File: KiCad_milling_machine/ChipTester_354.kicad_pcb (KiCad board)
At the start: 2 copper layers, 172 x 61.5 mm, 55 parts, among them U1 TLE2426xP, U2 L7805, U3 TLE2426xP, U4 TLE2426xP, U5 MCP6002-xP

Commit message: Removed Switch
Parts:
- removed C4: 1 µF, Capacitor_THT:CP_Radial_D5.0mm_P2.00mm
- removed S2: 100SP3T2B4M6RE, 100SP3T2B4M6RE:100SP3T2B4M6RE
- removed TP6: 4.5/2.25V VGND, TestPoint:TestPoint_Pad_D2.0mm
- removed U3: TLE2426xP, Package_DIP:DIP-8_W7.62mm
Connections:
- D11 pad 1: /2.5 VGND -> Net-(D10-A)
- D11 pad 2: Net-(D10-A) -> /2.5 VGND
- D13 pad 1: /2.5 VGND -> Net-(D12-A)
- D13 pad 2: Net-(D12-A) -> /2.5 VGND
- D3 pad 1: /CHIP_GND -> Net-(D2-A)
- D3 pad 2: Net-(D2-A) -> /CHIP_GND
- D5 pad 1: /CHIP_GND -> Net-(D4-A)
- D5 pad 2: Net-(D4-A) -> /CHIP_GND
- D9 pad 1: /2.5 VGND -> Net-(D8-A)
- D9 pad 2: Net-(D8-A) -> /2.5 VGND
- TP3 pad 1: /PWR Supply/VDIV -> /CHIP_GND
- U1 pad 1: /PWR Supply/VDIV -> /CHIP_GND
- U_T1 pad 7: /CHIP+ -> +9V
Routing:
- net /PWR Supply/VDIV: track 49.2 -> 0.00 mm
- net /CHIP_GND: track 56.7 -> 85.3 mm, vias 0 -> 1
- net /CHIP+: track 26.8 -> 0.00 mm
- net +9V: track 171.7 -> 185.6 mm
- net Net-(U3-NOISE_REDUCTION): track 3.76 -> 0.00 mm

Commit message: Ground inverting input of AD/INA circuit
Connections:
- U_T1 pad 2: unconnected-(U_T1---Pad2) -> GND
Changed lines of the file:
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@@
 	(net 34 "unconnected-(U5B-+-Pad5)")
 	(net 35 "unconnected-(U5B---Pad6)")
-	(net 36 "unconnected-(U_T1---Pad2)")
-	(net 37 "unconnected-(U_T1-Rg-Pad1)")
-	(net 38 "unconnected-(U_T1-Rg-Pad8)")
-	(net 39 "unconnected-(S1-Pad4)")
-	(net 40 "unconnected-(S1-Pad1)")
-	(net 41 "unconnected-(S1-PadS2)")
-	(net 42 "unconnected-(S1-PadS1)")
-	(net 43 "/AD623 and INA126/AD_O")
-	(net 44 "/MCP6002 and IF353/MCPA_O")
-	(net 45 "/MCP6002 and IF353/MCPB_O")
+	(net 36 "unconnected-(U_T1-Rg-Pad1)")
+	(net 37 "unconnected-(U_T1-Rg-Pad8)")
+	(net 38 "unconnected-(S1-Pad4)")
+	(net 39 "unconnected-(S1-Pad1)")
+	(net 40 "unconnected-(S1-PadS2)")
+	(net 41 "unconnected-(S1-PadS1)")
+	(net 42 "/AD623 and INA126/AD_O")
+	(net 43 "/MCP6002 and IF353/MCPA_O")
+	(net 44 "/MCP6002 and IF353/MCPB_O")
 	(footprint "Capacitor_THT:C_Disc_D5.0mm_W2.5mm_P2.50mm"
 		(layer "F.Cu")
@@
 			(layers "*.Cu" "*.Mask")
 			(remove_unused_layers no)
-			(net 43 "/AD623 and INA126/AD_O")
+			(net 42 "/AD623 and INA126/AD_O")
 			(pintype "passive")
 		)
@@
 			(layers "*.Cu" "*.Mask")
 			(remove_unused_layers no)
-			(net 43 "/AD623 and INA126/AD_O")
+			(net 42 "/AD623 and INA126/AD_O")
 			(pinfunction "2")
 			(pintype "passive")
@@
 			(layers "*.Cu" "*.Mask")
 			(remove_unused_layers no)
-			(net 45 "/MCP6002 and IF353/MCPB_O")
+			(net 44 "/MCP6002 and IF353/MCPB_O")
 			(pintype "passive")
 		)
@@
 			(remove_unused_layers no)
 			(roundrect_rratio 0.15625)
-			(net 37 "unconnected-(U_T1-Rg-Pad1)")
+			(net 36 "unconnected-(U_T1-Rg-Pad1)")
 			(pinfunction "Rg")
 			(pintype "passive+no_connect")
@@
 			(layers "*.Cu" "*.Mask")
 			(remove_unused_layers no)
-			(net 36 "unconnected-(U_T1---Pad2)")
+			(net 1 "GND")
 			(pinfunction "-")
-			(pintype "input+no_connect")
+			(pintype "input")
 		)
 		(pad "3" thru_hole circle
@@
 			(layers "*.Cu" "*.Mask")
 			(remove_unused_layers no)
-			(net 43 "/AD623 and INA126/AD_O")
+			(net 42 "/AD623 and INA126/AD_O")
 			(pintype "output")
 		)
@@
 			(layers "*.Cu" "*.Mask")
 			(remove_unused_layers no)
-			(net 38 "unconnected-(U_T1-Rg-Pad8)")
+			(net 37 "unconnected-(U_T1-Rg-Pad8)")
 			(pinfunction "Rg")
 			(pintype "passive+no_connect")
@@
 			(layers "*.Cu" "*.Mask")
 			(remove_unused_layers no)
-			(net 40 "unconnected-(S1-Pad1)")
+			(net 39 "unconnected-(S1-Pad1)")
 			(pintype "passive+no_connect")
 			(solder_mask_margin 0.102)
@@
 			(layers "*.Cu" "*.Mask")
 			(remove_unused_layers no)
-			(net 39 "unconnected-(S1-Pad4)")
+			(net 38 "unconnected-(S1-Pad4)")
 			(pintype "passive+no_connect")
 			(solder_mask_margin 0.102)
@@
 			(layers "*.Cu" "*.Mask")
 			(remove_unused_layers no)
-			(net 42 "unconnected-(S1-PadS1)")
+			(net 41 "unconnected-(S1-PadS1)")
 			(pintype "free+no_connect")
 			(solder_mask_margin 0.102)
@@
 			(layers "*.Cu" "*.Mask")
 			(remove_unused_layers no)
-			(net 41 "unconnected-(S1-PadS2)")
+			(net 40 "unconnected-(S1-PadS2)")
 			(pintype "free+no_connect")
 			(solder_mask_margin 0.102)
@@
 			(layers "*.Cu" "*.Mask")
 			(remove_unused_layers no)
-			(net 44 "/MCP6002 and IF353/MCPA_O")
+			(net 43 "/MCP6002 and IF353/MCPA_O")
 			(pintype "passive")
 		)
@@
 			(layers "*.Cu" "*.Mask")
 			(remove_unused_layers no)
-			(net 44 "/MCP6002 and IF353/MCPA_O")
+			(net 43 "/MCP6002 and IF353/MCPA_O")
 			(pinfunction "Pin_2")
 			(pintype "passive")
@@
 			(layers "*.Cu" "*.Mask")
 			(remove_unused_layers no)
-			(net 45 "/MCP6002 and IF353/MCPB_O")
+			(net 44 "/MCP6002 and IF353/MCPB_O")
 			(pinfunction "Pin_3")
 			(pintype "passive")
@@
 			(remove_unused_layers no)
 			(roundrect_rratio 0.15625)
-			(net 44 "/MCP6002 and IF353/MCPA_O")
+			(net 43 "/MCP6002 and IF353/MCPA_O")
 			(pintype "output")
 		)
@@
 			(layers "*.Cu" "*.Mask")
 			(remove_unused_layers no)
-			(net 44 "/MCP6002 and IF353/MCPA_O")
+			(net 43 "/MCP6002 and IF353/MCPA_O")
 			(pinfunction "-")
 			(pintype "input")
@@
 			(layers "*.Cu" "*.Mask")
 			(remove_unused_layers no)
-			(net 45 "/MCP6002 and IF353/MCPB_O")
+			(net 44 "/MCP6002 and IF353/MCPB_O")
 			(pinfunction "-")
 			(pintype "input")
@@
 			(layers "*.Cu" "*.Mask")
 			(remove_unused_layers no)
-			(net 45 "/MCP6002 and IF353/MCPB_O")
+			(net 44 "/MCP6002 and IF353/MCPB_O")
 			(pintype "output")
 		)
@@
 		(width 1)
 		(layer "F.Cu")
-		(net 43)
+		(net 42)
 	)
 	(segment
@@
 		(width 1)
 		(layer "F.Cu")
-		(net 43)
+		(net 42)
 	)
 	(segment
@@
 		(width 1)
 		(layer "F.Cu")
-		(net 43)
+		(net 42)
 	)
 	(segment
@@
 		(width 1)
 		(layer "F.Cu")
-		(net 43)
+		(net 42)
 	)
 	(segment
@@
 		(width 1)
 		(layer "F.Cu")
-		(net 43)
+		(net 42)
 	)
 	(segment
@@
 		(width 1)
 		(layer "F.Cu")
-		(net 44)
+		(net 43)
 	)
 	(segment
@@
 		(width 1)
 		(layer "F.Cu")
-		(net 44)
+		(net 43)
 	)
 	(segment
@@
 		(width 1)
 		(layer "F.Cu")
-		(net 44)
+		(net 43)
 	)
 	(segment
@@
 		(width 1)
 		(layer "B.Cu")
-		(net 44)
+		(net 43)
 	)
 	(segment
@@
 		(width 1)
 		(layer "B.Cu")
-		(net 44)
+		(net 43)
 	)
 	(segment
@@
 		(width 1)
 		(layer "B.Cu")
-		(net 44)
+		(net 43)
 	)
 	(segment
@@
 		(width 1)
 		(layer "B.Cu")
-		(net 44)
+		(net 43)
 	)
 	(segment
@@
 		(width 1)
 		(layer "F.Cu")
-		(net 45)
+		(net 44)
 	)
 	(segment
@@
 		(width 1)
 		(layer "B.Cu")
-		(net 45)
+		(net 44)
 	)
 	(segment
@@
 		(width 1)
 		(layer "B.Cu")
-		(net 45)
+		(net 44)
 	)
 	(segment
@@
 		(width 1)
 		(layer "B.Cu")
-		(net 45)
+		(net 44)
 	)
 	(segment
@@
 		(width 1)
 		(layer "B.Cu")
-		(net 45)
+		(net 44)
 	)
 	(segment
@@
 		(width 1)
 		(layer "B.Cu")
-		(net 45)
+		(net 44)
 	)
 	(segment
@@
 		(width 1)
 		(layer "B.Cu")
-		(net 45)
+		(net 44)
 	)
 	(segment
@@
 		(width 1)
 		(layer "B.Cu")
-		(net 45)
+		(net 44)
 	)
 	(zone

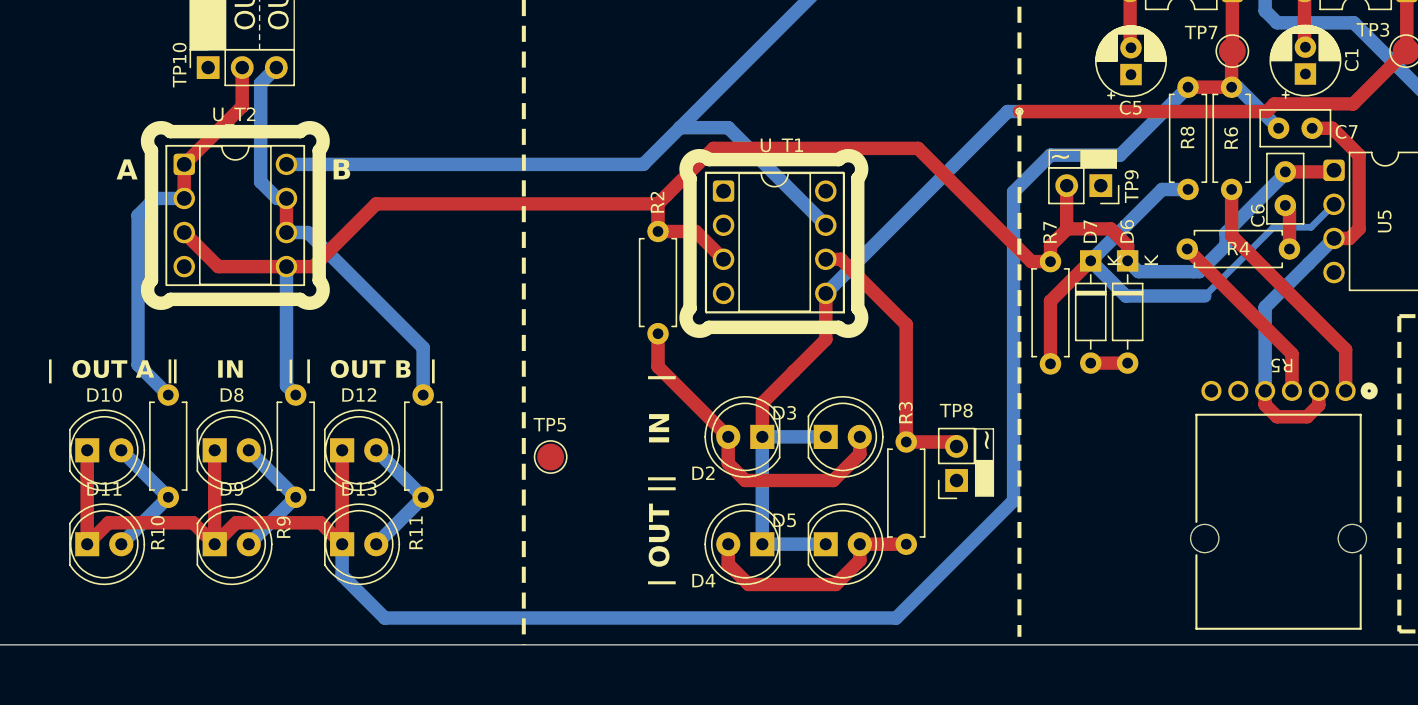
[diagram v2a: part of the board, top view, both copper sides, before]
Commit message: grounded LEDs to allow for sufficient voltage blinking difference
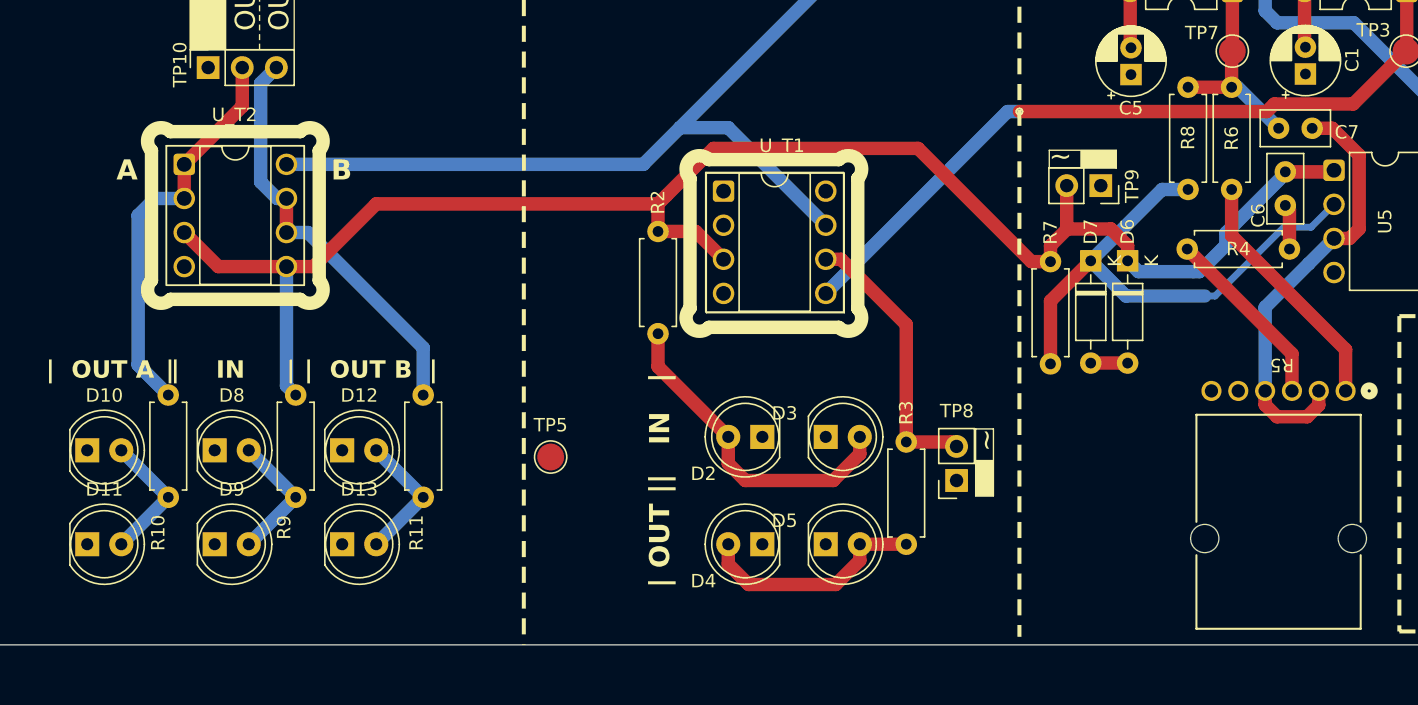
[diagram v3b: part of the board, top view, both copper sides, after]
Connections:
- D10 pad 1: /2.5 VGND -> GND
- D11 pad 1: Net-(D10-A) -> GND
- D11 pad 2: /2.5 VGND -> Net-(D10-A)
- D12 pad 1: /2.5 VGND -> GND
- D13 pad 1: Net-(D12-A) -> GND
- D13 pad 2: /2.5 VGND -> Net-(D12-A)
- D2 pad 1: /CHIP_GND -> GND
- D3 pad 1: Net-(D2-A) -> GND
- D3 pad 2: /CHIP_GND -> Net-(D2-A)
- D4 pad 1: /CHIP_GND -> GND
- D5 pad 1: Net-(D4-A) -> GND
- D5 pad 2: /CHIP_GND -> Net-(D4-A)
- D8 pad 1: /2.5 VGND -> GND
- D9 pad 1: Net-(D8-A) -> GND
- D9 pad 2: /2.5 VGND -> Net-(D8-A)
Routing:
- net /2.5 VGND: track 154.4 -> 15.2 mm
- net /CHIP_GND: track 85.3 -> 55.2 mm
